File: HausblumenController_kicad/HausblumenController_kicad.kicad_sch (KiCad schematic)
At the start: 8 parts, among them J1 Conn_ST_STDC14, U1 STM32F401CCUx, Y1 24MHz, Y2 32.768kHz

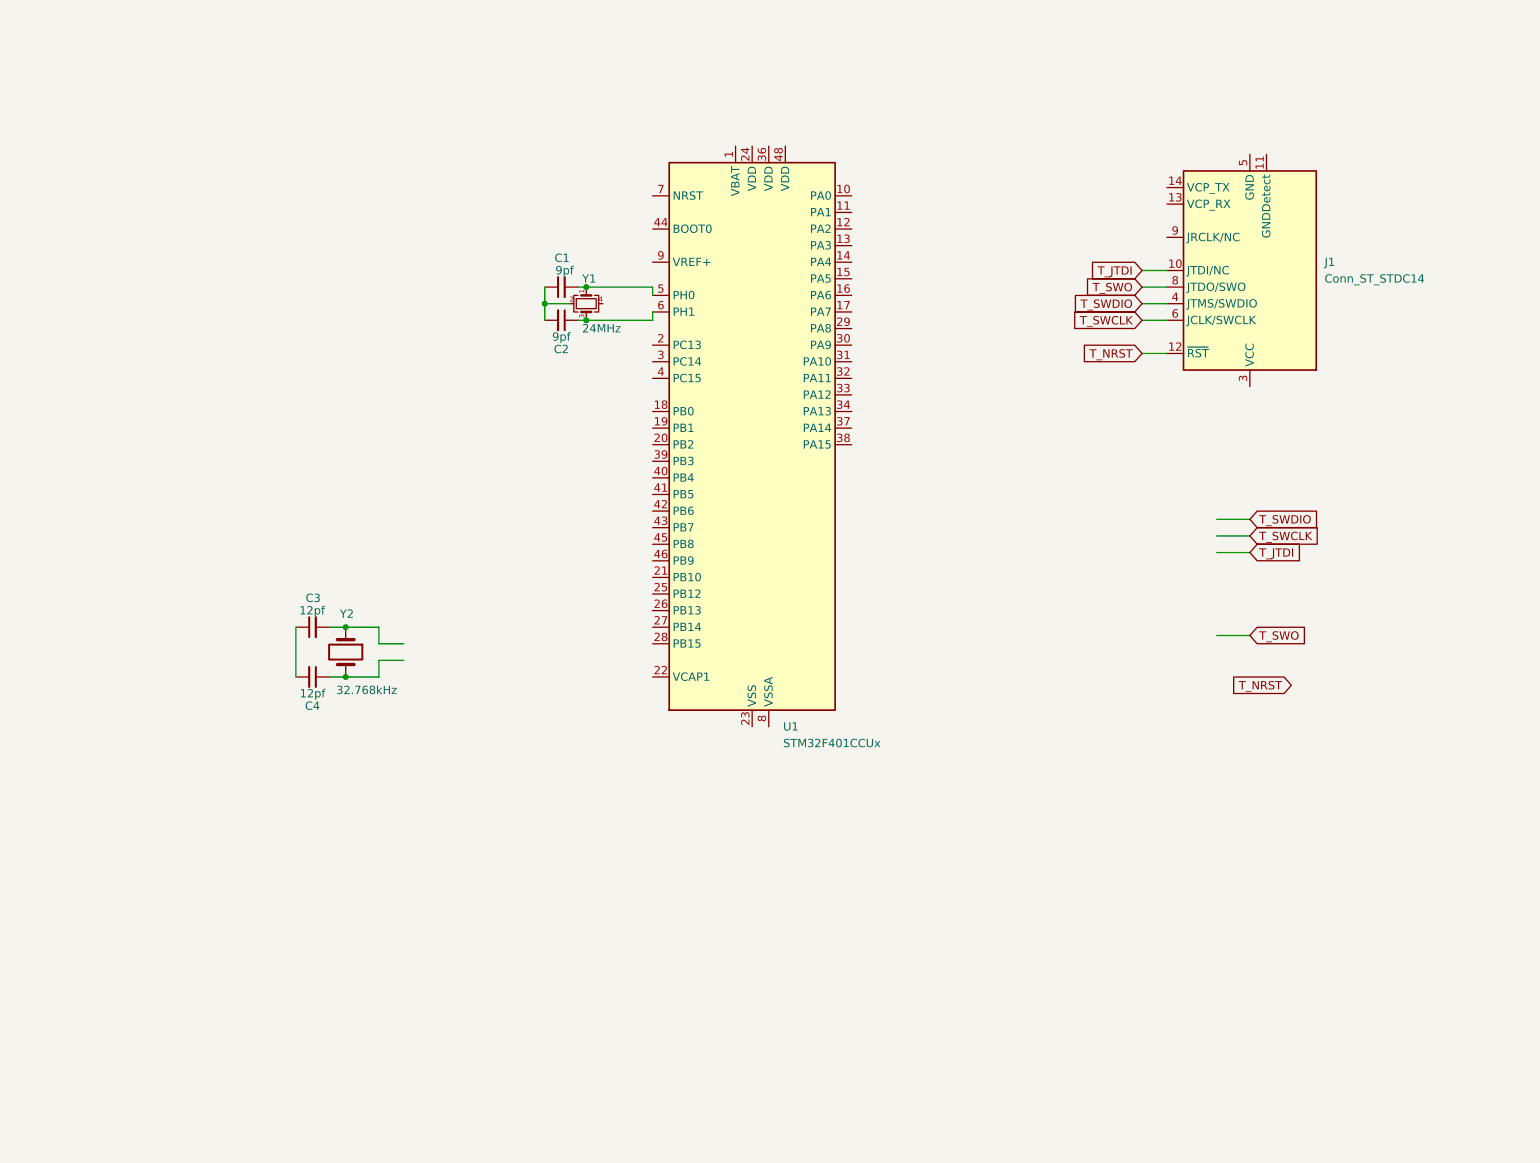
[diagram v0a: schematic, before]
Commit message: targeted MCU and base elements
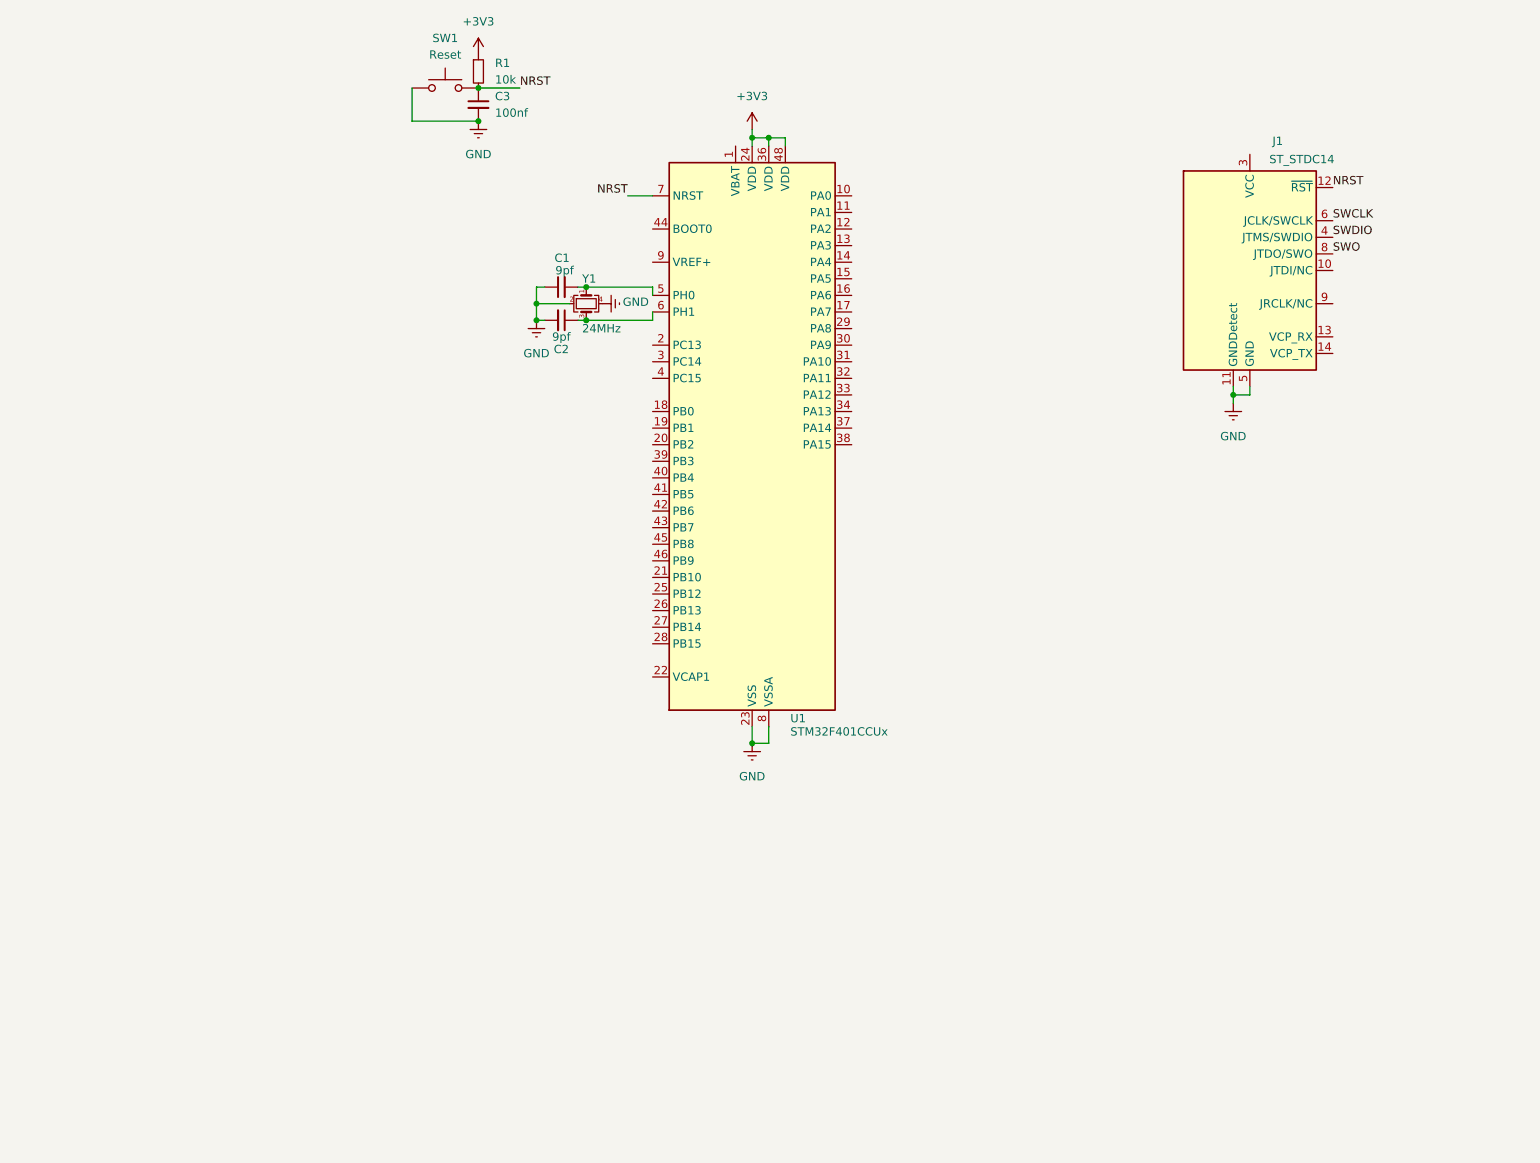
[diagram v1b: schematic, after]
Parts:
- removed C4: 12pf, Capacitor_SMD:C_0603_1608Metric, symbol Device:C_Small
- removed Y2: 32.768kHz, Crystal:Crystal_SMD_2012-2Pin_2.0x1.2mm, symbol Device:Crystal
- added R1: 10k, Capacitor_SMD:C_0402_1005Metric, symbol Device:R_Small
- added SW1: Reset, Button_Switch_SMD:SW_Tactile_SPST_NO_Straight_CK_PTS636Sx25SMTRLFS, symbol Switch:SW_Push
- C1, C2: footprint Capacitor_SMD:C_0603_1608Metric -> Capacitor_SMD:C_0201_0603Metric
- C3: value 12pf -> 100nf; footprint Capacitor_SMD:C_0603_1608Metric -> Capacitor_SMD:C_0402_1005Metric
- J1: value Conn_ST_STDC14 -> ST_STDC14
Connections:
- net T_NRST is gone; now on net NRST: J1.12 (~{RST})
- net GND: now reaches C1.1, C2.2, Y1.2
- net GND: now also C3.2, J1.11 (GNDDetect), J1.5 (GND), J1.7 (GND), U1.23 (VSS), U1.35 (VSS), U1.47 (VSS), U1.49 (VSS), U1.8 (VSSA), Y1.4, SW1.1
- net +3V3: now reaches U1.24 (VDD)
- net +3V3: now also U1.36 (VDD), U1.48 (VDD), R1.1
- net NRST: now reaches U1.7 (NRST)
- net NRST: now also C3.1, R1.2, SW1.2
- net T_JTDI: no longer names the net of J1.10 (JTDI/NC)
- net T_SWCLK renamed SWCLK
- net T_SWDIO renamed SWDIO
- net T_SWO renamed SWO
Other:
- moved on the sheet: J1

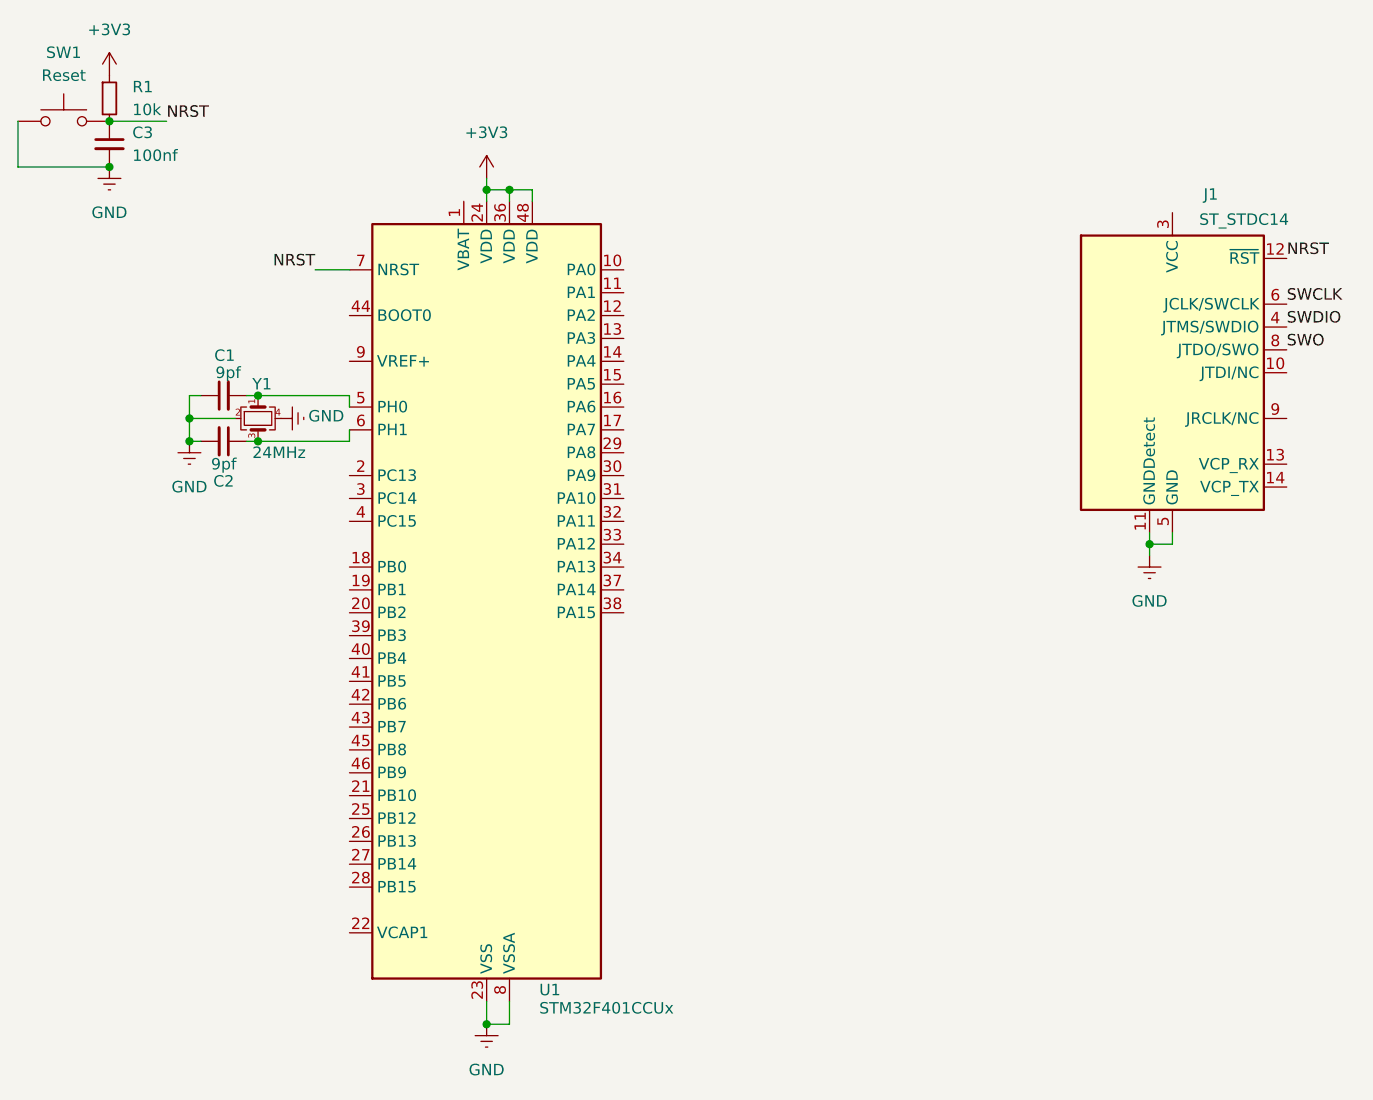
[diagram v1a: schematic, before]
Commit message: added BlackPill
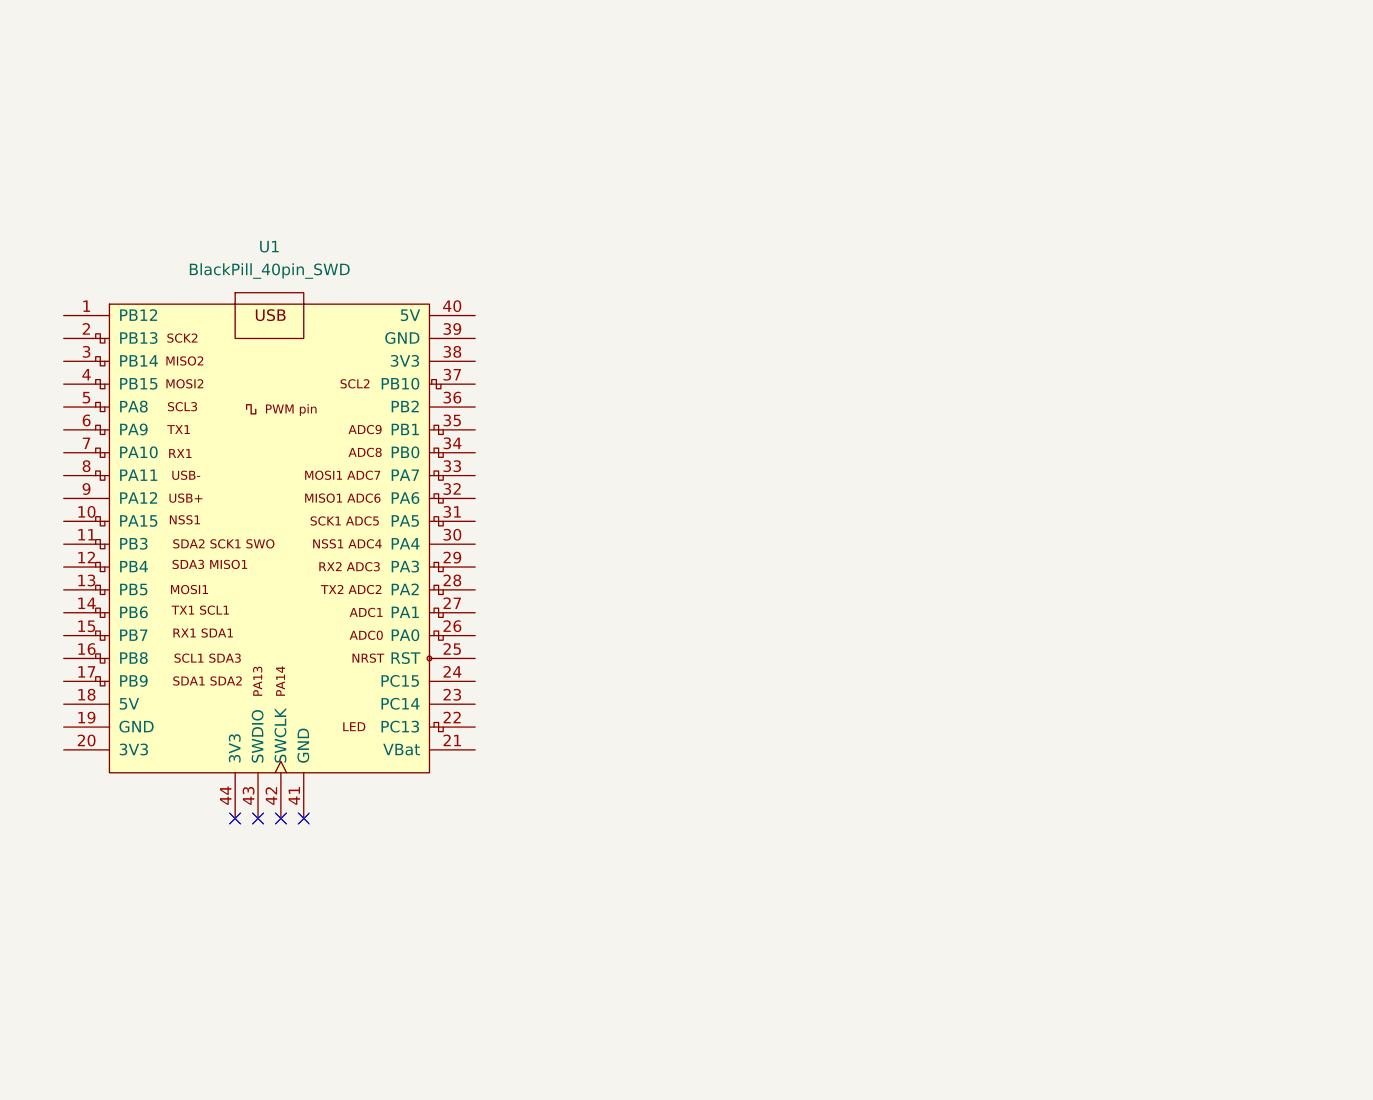
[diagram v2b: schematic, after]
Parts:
- removed C1, C2: 9pf, Capacitor_SMD:C_0201_0603Metric, symbol Device:C_Small
- removed C3: 100nf, Capacitor_SMD:C_0402_1005Metric, symbol Device:C_Small
- removed J1: ST_STDC14, symbol Connector:Conn_ST_STDC14
- removed R1: 10k, Capacitor_SMD:C_0402_1005Metric, symbol Device:R_Small
- removed SW1: Reset, Button_Switch_SMD:SW_Tactile_SPST_NO_Straight_CK_PTS636Sx25SMTRLFS, symbol Switch:SW_Push
- removed U1: STM32F401CCUx, Package_DFN_QFN:QFN-48-1EP_7x7mm_P0.5mm_EP5.6x5.6mm, symbol MCU_ST_STM32F4:STM32F401CCUx
- removed Y1: 24MHz, Crystal:Crystal_SMD_3225-4Pin_3.2x2.5mm, symbol Device:Crystal_GND24_Small
- added U1: BlackPill_40pin_SWD, WeAct:BlackPill_40pin_SWD, symbol WeAct:BlackPill_40pin_SWD
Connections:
- no-connect marks 0 -> 4

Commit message: chore: .gitignore update
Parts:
- added Q1: IRLML2402, Package_TO_SOT_SMD:SOT-23, symbol Transistor_FET:IRLML2060
- added R1: 10k, Resistor_SMD:R_0603_1608Metric, symbol Device:R_Small
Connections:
- new net: Q1.1 (G), R1.1
- new net: Q1.2 (S), R1.2
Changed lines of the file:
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@@
 		(at 107.95 107.95)
+	)
+	(wire
+		(pts
+			(xy 167.64 76.2) (xy 176.53 76.2)
+		)
+		(stroke
+			(width 0)
+			(type default)
+		)
+	)
+	(wire
+		(pts
+			(xy 167.64 71.12) (xy 168.91 71.12)
+		)
+		(stroke
+			(width 0)
+			(type default)
+		)
 	)
 	(symbol
@@
 					(unit 1)
 				)
+			)
+		)
+	)
+	(symbol
+		(lib_id "Device:R_Small")
+		(at 167.64 73.66 0)
+		(unit 1)
+		(exclude_from_sim no)
+		(in_bom yes)
+		(on_board yes)
+		(dnp no)
+		(fields_autoplaced yes)
+		(property "Reference" "R1"
+			(at 170.18 72.3899 0)
+			(effects
+				(font
+					(size 1.27 1.27)
+				)
+				(justify left)
+			)
+		)
+		(property "Value" "10k"
+			(at 170.18 74.9299 0)
+			(effects
+				(font
+					(size 1.27 1.27)
+				)
+				(justify left)
+			)
+		)
+		(property "Footprint" "Resistor_SMD:R_0603_1608Metric"
+			(at 167.64 73.66 0)
+			(effects
+				(font
+					(size 1.27 1.27)
+				)
+				(hide yes)
+			)
+		)
+		(property "Datasheet" "~"
+			(at 167.64 73.66 0)
+			(effects
+				(font
+					(size 1.27 1.27)
+				)
+				(hide yes)
+			)
+		)
+		(property "Description" "Resistor, small symbol"
+			(at 167.64 73.66 0)
+			(effects
+				(font
+					(size 1.27 1.27)
+				)
+				(hide yes)
+			)
+		)
+		(pin "2"
+		)
+		(pin "1"
+		)
+		(instances
+			(project ""
+				(path "/763b7ff5-a573-497b-9e68-3c06692609a4"
+					(reference "R1")
+					(unit 1)
+				)
+			)
+		)
+	)
+	(symbol
+		(lib_id "Transistor_FET:IRLML2060")
+		(at 173.99 71.12 0)
+		(unit 1)
+		(exclude_from_sim no)
+		(in_bom yes)
+		(on_board yes)
+		(dnp no)
+		(fields_autoplaced yes)
+		(property "Reference" "Q1"
+			(at 180.34 69.8499 0)
+			(effects
+				(font
+					(size 1.27 1.27)
+				)
+				(justify left)
+			)
+		)
+		(property "Value" "IRLML2402"
+			(at 180.34 72.3899 0)
+			(effects
+				(font
+					(size 1.27 1.27)
+				)
+				(justify left)
+			)
+		)
+		(property "Footprint" "Package_TO_SOT_SMD:SOT-23"
+			(at 179.07 73.025 0)
+			(effects
+				(font
+					(size 1.27 1.27)
+					(italic yes)
+				)
+				(justify left)
+				(hide yes)
+			)
+		)
+		(property "Datasheet" "https://www.infineon.com/dgdl/irlml2060pbf.pdf?fileId=5546d462533600a401535664b7fb25ee"
+			(at 179.07 74.93 0)
+			(effects
+				(font
+					(size 1.27 1.27)
+				)
+				(justify left)
+				(hide yes)
+			)
+		)
+		(property "Description" "1.2A Id, 60V Vds, 480mOhm Rds, N-Channel HEXFET Power MOSFET, SOT-23"
+			(at 173.99 71.12 0)
+			(effects
+				(font
+					(size 1.27 1.27)
+				)
+				(hide yes)
+			)
+		)
+		(pin "2"
+		)
+		(pin "1"
+		)
+		(pin "3"
+		)
+		(instances
+			(project ""
+				(path "/763b7ff5-a573-497b-9e68-3c06692609a4"
+					(reference "Q1")
+					(unit 1)
+				)
